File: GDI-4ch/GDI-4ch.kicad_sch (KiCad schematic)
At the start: 255 parts, among them J1 Conn_02x02_Odd_Even, J2 FTSH-107-01-F-DV-K, J3 TC2030, J4 Conn_01x06, J5 Conn_01x04, P1 368255-2, P10 Pad, P11 Pad, P18 Pad, P19 Pad, P2 Pad, P20 Pad, P25 Pad, P3 Pad, P32 Pad, P36 Pad, P4 Pad, P5 Pad, P6 Pad, P7 Pad, P8 Pad, P9 Pad, Q1 BUK9230-100B, Q10 BUK9230-100B, Q11 BUK9230-100B, Q12 BUK9230-100B, Q13 AOD4185, Q14 VND14NV04TR-E, Q15 VND14NV04TR-E, Q2 BUK9230-100B, Q3 BUK9230-100B, Q4 BUK9230-100B, Q5 BUK9230-100B, Q6 BUK9230-100B, Q7 BUK9230-100B, Q8 BUK9230-100B, Q9 BUK9230-100B, U1 MC33816, U2 TJA1051T-3, U3 LM78M05_TO252, U4 74HC14, U5 XC6206P332MR, U6 MCP6004, U7 STM32F103C8Tx, Y2 1MHz

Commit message: PCB update 6ch
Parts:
- removed R92: DNP, hellen-one-common:PAD-0805-PAD, symbol hellen-one-common:Jumper-Pad-Pad
- removed R93: Jumper-Pad-Pad, hellen-one-common:PAD-0805-PAD, symbol hellen-one-common:Jumper-Pad-Pad
- added C89: 1000pF, Capacitor_SMD:C_0603_1608Metric, symbol Device:C
- added D19: STPS2H100UY, Diode_SMD:D_SMB, symbol Device:D_Schottky_Small
- added Q16: BUK9230-100B, Package_TO_SOT_SMD:TO-252-2, symbol Device:Q_NMOS_GDS
- added R37: DNP, hellen-one-common:PAD-0805-PAD, symbol hellen-one-common:Jumper-Pad-Pad
- added R41: Jumper-Pad-Pad, hellen-one-common:PAD-0805-PAD, symbol hellen-one-common:Jumper-Pad-Pad
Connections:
- net +BATT: now also D16.1 (K)
- net L6: now also D19.2 (A), Q16.2 (D), R41.1; no longer C67.2, D16.2 (A), Q12.2 (D), R87.2, U1.33 (D_LS6)
- net Vdrive: now also D19.1 (K)
- net VSENSE2: now reaches C58.1, C61.1, Q10.3 (S), Q9.3 (S), R22.1
- net VSENSE2: now also C89.1, Q16.3 (S)
- net at C63.2, Q12.1 (G), R20.2: now also C89.2, Q16.1 (G)
- net at C63.1, Q12.3 (S), R26.1: no longer C87.1, Q1.3 (S)
- net VSENSE1: now reaches C54.1, C55.1, Q7.3 (S), Q8.3 (S), R21.1
- net VSENSE1: now also C87.1, Q1.3 (S)
- new net: R37.2, R41.2, U1.33 (D_LS6)
- new net L6PUMP: C67.2, D16.2 (A), Q12.2 (D), R37.1, R87.2
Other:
- note removed: "PUMP"
- moved on the sheet: C10, C11, C12, C13, C14, C15, C16, C17, C21, C22, C23, C24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

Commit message: Fab preview
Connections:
- no-connect marks 91 -> 92
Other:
- note removed: "INJ"
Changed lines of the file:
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@@
   (title_block
     (title "GDI 4ch")
-    (date "2022-06-30")
+    (date "2022-07-07")
     (rev "rev. c")
     (company "rusEFI.com")
@@
   (no_connect (at 546.1 129.54))
   (no_connect (at 556.26 106.68))
+  (no_connect (at 482.6 143.51))
   (no_connect (at 44.45 314.96))
   (no_connect (at 44.45 317.5))
@@
     (effects (font (size 1.524 1.524)) (justify left bottom))
   )
-  (text "INJ" (at 312.42 320.04 0)
-    (effects (font (size 1.524 1.524)) (justify left bottom))
-  )

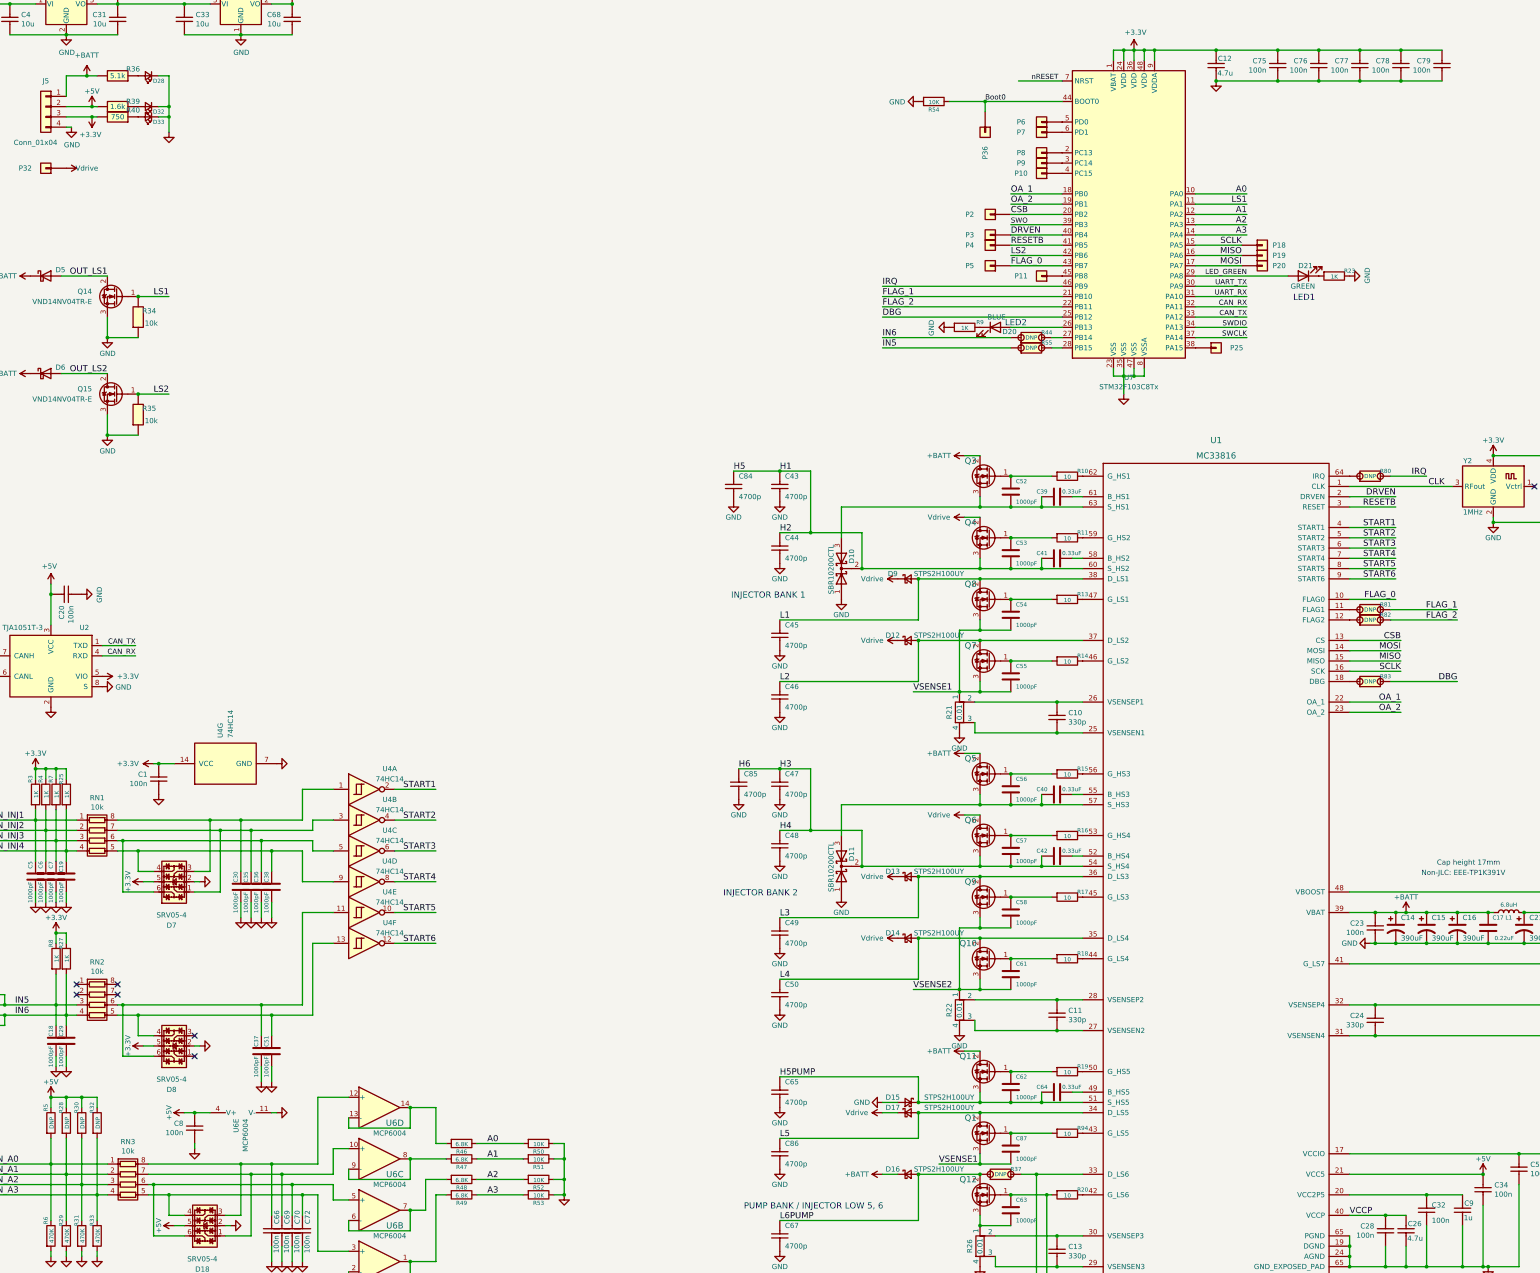
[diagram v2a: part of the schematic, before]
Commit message: Added STM32 8MHz crystal
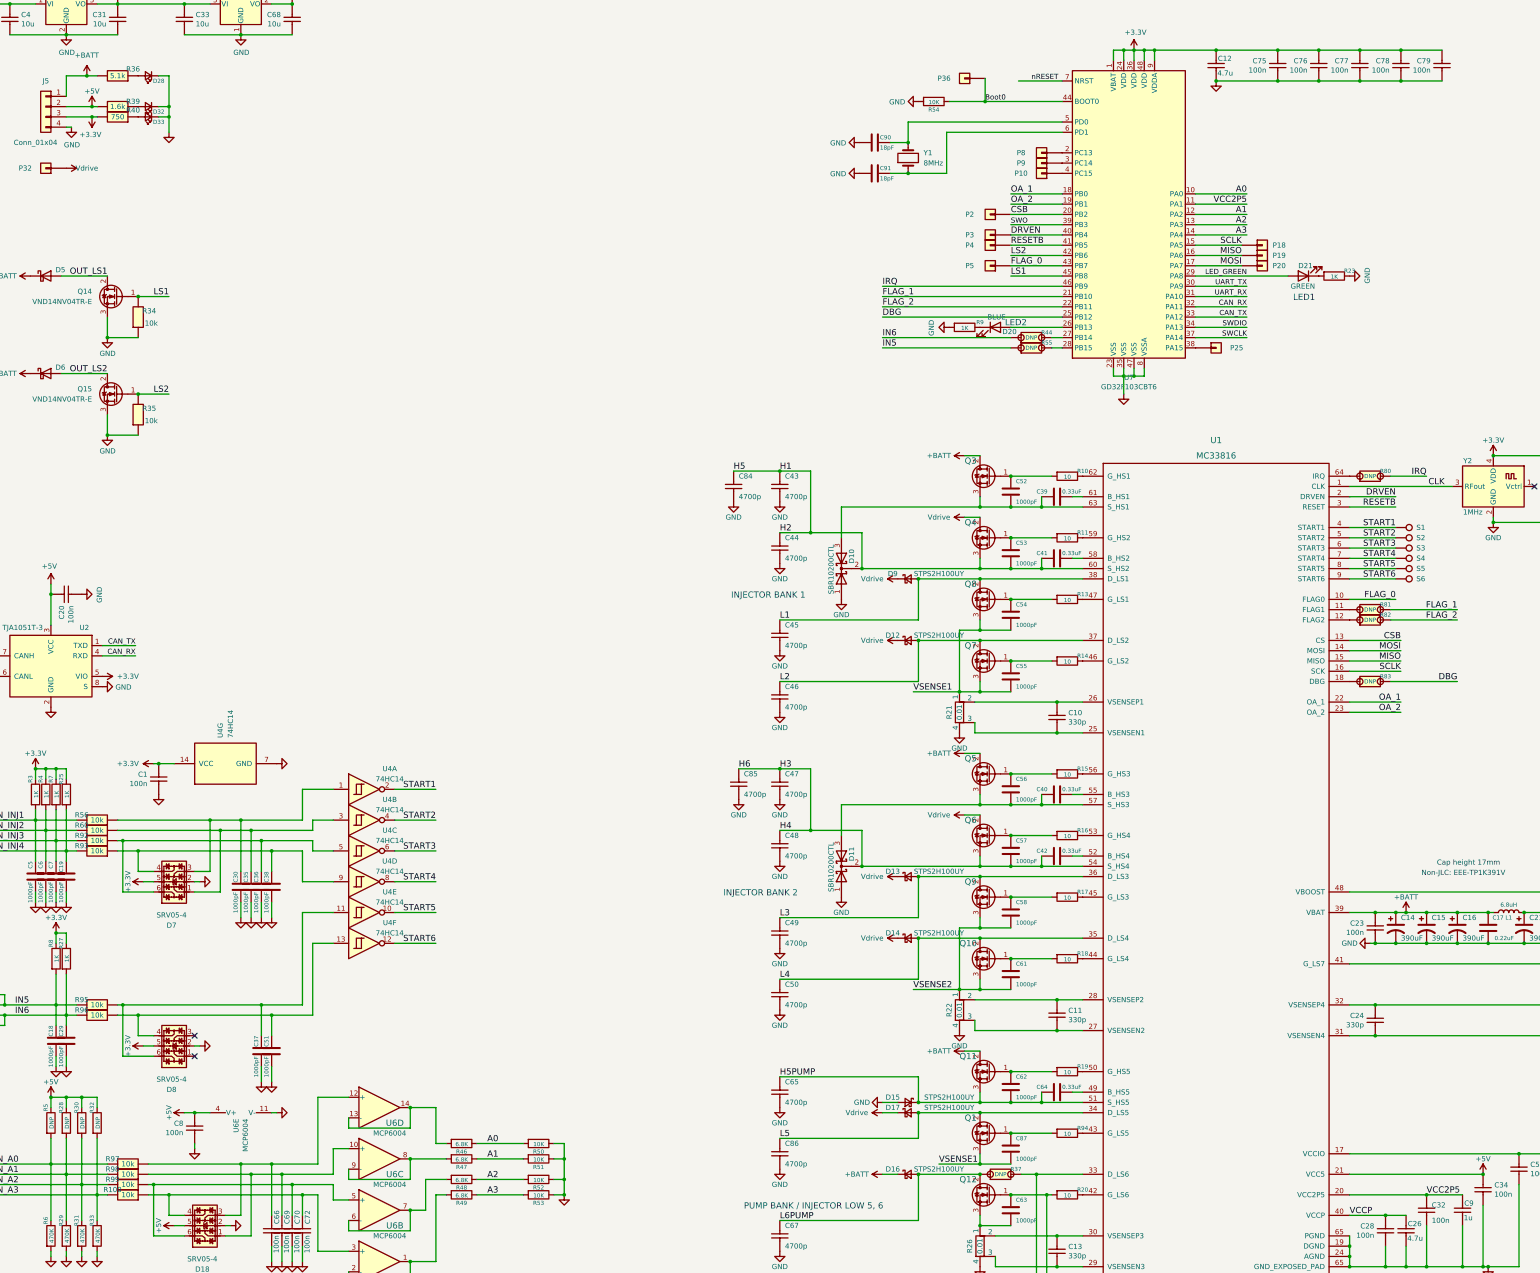
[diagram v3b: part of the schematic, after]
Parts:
- removed P11, P6, P7: Pad, hellen-one-common:PAD-TH, symbol hellen-one-common:Pad
- removed RN1, RN2, RN3: 10k, Resistor_SMD:R_Array_Convex_4x0603, symbol Device:R_Pack04
- added C90, C91: 18pF, Capacitor_SMD:C_0603_1608Metric, symbol Device:C
- added R100, R56, R60, R92, R93, R95, R96, R97, R98, R99: 10k, hellen-one-common:R0603, symbol hellen-one-common:Res
- added S1, S2, S3, S4, S5, S6: TestPoint, TestPoint:TestPoint_Pad_D1.5mm, symbol Connector:TestPoint
- added Y1: 8MHz, Crystal:Crystal_SMD_HC49-SD, symbol Device:Crystal
- U7: value STM32F103C8Tx -> GD32F103CBT6; LCSC C8734 -> C77979
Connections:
- net GND: now also C90.2, C91.2
- net IN5: now also R95.2
- net IN6: now also R96.2
- net IN_A0: now also R97.2
- net IN_A1: now also R98.2
- net IN_A2: now also R99.2
- net IN_A3: now also R100.2
- net IN_INJ1: now also R56.2
- net IN_INJ2: now also R60.2
- net IN_INJ3: now also R92.2
- net IN_INJ4: now also R93.2
- net LS1: now also U7.45 (PB8); no longer U7.11 (PA1)
- net START1: now also S1.1
- net START2: now also S2.1
- net START3: now also S3.1
- net START4: now also S4.1
- net START5: now also S5.1
- net START6: now also S6.1
- net at C51.2, D8.4, U4.13: now also R96.1
- net at C72.2, D18.4, U6.3 (+): now also R100.1
- net at C35.2, D7.1, U4.3: now also R60.1
- net at C30.2, D7.3, U4.1: now also R56.1
- net at C38.2, D7.4, U4.9: now also R93.1
- net at C36.2, D7.6, U4.5: now also R92.1
- net at U7.6 (PD1): now also C91.1, Y1.1
- net at C37.2, D8.6, U4.11: now also R95.1
- net VCC2P5: now reaches C32.2, C9.2, U1.20 (VCC2P5)
- net VCC2P5: now also U7.11 (PA1)
- net at C69.2, D18.1, U6.10 (+): now also R98.1
- net at C66.2, D18.3, U6.12 (+): now also R97.1
- net at C70.2, D18.6, U6.5 (+): now also R99.1
- net at U7.5 (PD0): now also C90.1, Y1.2
- no-connect marks 92 -> 88
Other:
- moved on the sheet: P36

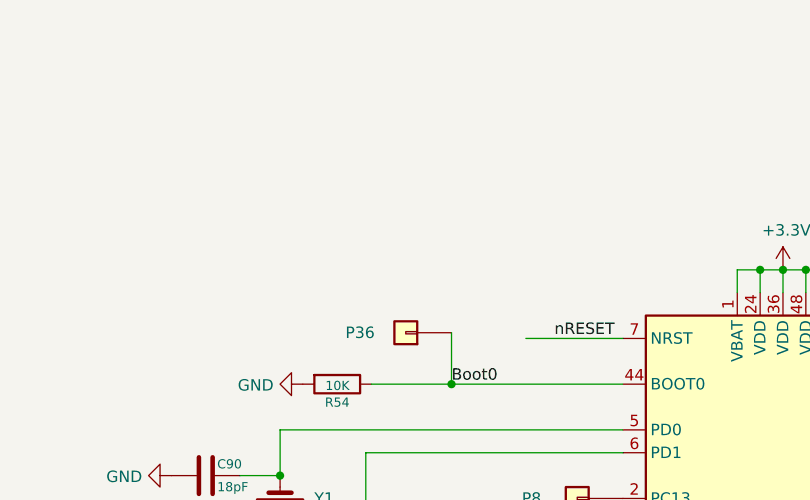
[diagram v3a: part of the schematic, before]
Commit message: BOOT and RST buttons
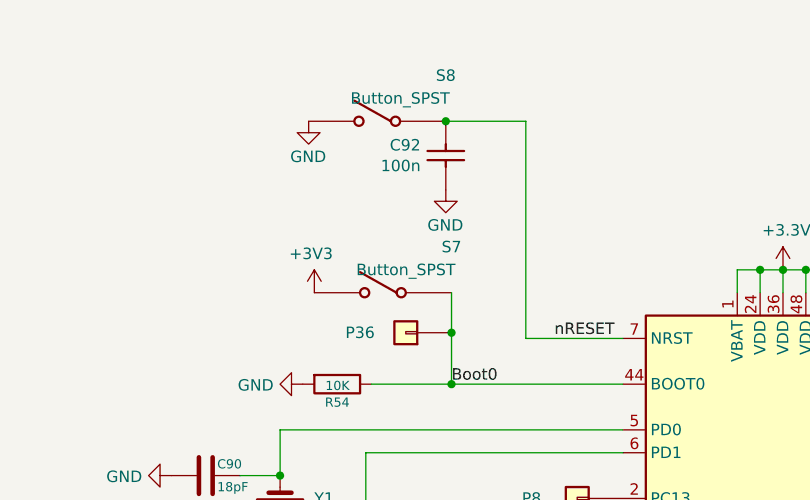
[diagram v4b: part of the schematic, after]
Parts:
- added C92: 100n, hellen-one-common:C0603, symbol hellen-one-common:Cap
- added S7, S8: Button_SPST, hellen-one-common:SMD-2_2.9x3.9x1.7, symbol hellen-one-common:Button_SPST
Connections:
- net +3V3: now also S7.2
- net Boot0: now also S7.1
- net GND: now also C92.1, S8.2
- net nRESET: now also C92.2, S8.1
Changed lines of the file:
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@@
   (title_block
     (title "GDI 4ch")
-    (date "2022-07-07")
+    (date "2022-07-18")
     (rev "rev. c")
     (company "rusEFI.com")
@@
   (junction (at 204.47 309.88) (diameter 0) (color 0 0 0 0)
   )
+  (junction (at 346.71 42.545) (diameter 0) (color 0 0 0 0)
+  )
   (junction (at 162.56 311.15) (diameter 0) (color 0 0 0 0)
   )
@@
   (junction (at 167.64 231.14) (diameter 0) (color 0 0 0 0)
   )
+  (junction (at 346.075 19.05) (diameter 0) (color 0 0 0 0)
+  )
   (junction (at 455.93 336.55) (diameter 0) (color 0 0 0 0)
   )
@@
     (stroke (width 0) (type default) (color 0 0 0 0))
   )
+  (wire (pts (xy 354.965 19.05) (xy 354.965 43.18))
+    (stroke (width 0) (type default) (color 0 0 0 0))
+  )
   (wire (pts (xy 321.31 106.68) (xy 353.06 106.68))
     (stroke (width 0) (type default) (color 0 0 0 0))
@@
     (stroke (width 0) (type default) (color 0 0 0 0))
   )
+  (wire (pts (xy 346.075 19.05) (xy 354.965 19.05))
+    (stroke (width 0) (type default) (color 0 0 0 0))
+  )
   (wire (pts (xy 556.26 82.55) (xy 565.15 82.55))
     (stroke (width 0) (type default) (color 0 0 0 0))
@@
     (stroke (width 0) (type default) (color 0 0 0 0))
   )
+  (wire (pts (xy 346.71 38.1) (xy 346.71 42.545))
+    (stroke (width 0) (type default) (color 0 0 0 0))
+  )
   (wire (pts (xy 127 24.13) (xy 132.08 24.13))
     (stroke (width 0) (type default) (color 0 0 0 0))
@@
     (pin "1")
   )
+  (symbol (lib_id "power:+3V3") (at 331.47 38.1 0) (mirror y) (unit 1)
+    (in_bom yes) (on_board yes)
+    (property "Reference" "#PWR079" (id 0) (at 331.47 41.91 0)
+      (effects (font (size 1.27 1.27)) hide)
+    )
+    (property "Value" "+3V3" (id 1) (at 331.1017 33.7756 0))
+    (property "Footprint" "" (id 2) (at 331.47 38.1 0)
+      (effects (font (size 1.27 1.27)) hide)
+    )
+    (property "Datasheet" "" (id 3) (at 331.47 38.1 0)
+      (effects (font (size 1.27 1.27)) hide)
+    )
+    (pin "1")
+  )
   (symbol (lib_id "Device:D_Schottky_Small") (at 327.66 344.17 0) (unit 1)
     (in_bom yes) (on_board yes)
@@
     (pin "2")
   )
+  (symbol (lib_id "hellen-one-common:Cap") (at 346.075 22.86 270) (mirror x) (unit 1)
+    (in_bom yes) (on_board yes)
+    (property "Reference" "C92" (id 0) (at 343.2809 21.7106 90)
+      (effects (font (size 1.27 1.27)) (justify right))
+    )
+    (property "Value" "100n" (id 1) (at 343.2809 24.0093 90)
+      (effects (font (size 1.27 1.27)) (justify right))
+    )
+    (property "Footprint" "hellen-one-common:C0603" (id 2) (at 342.265 25.4 0)
+      (effects (font (size 1.27 1.27)) hide)
+    )
+    (property "Datasheet" "" (id 3) (at 346.075 26.67 90)
+      (effects (font (size 1.27 1.27)) hide)
+    )
+    (property "LCSC" "C14663" (id 4) (at 346.075 22.86 0)
+      (effects (font (size 1.27 1.27)) hide)
+    )
+    (pin "1")
+    (pin "2")
+  )
   (symbol (lib_id "power:+5V") (at 568.325 60.325 0) (unit 1)
     (in_bom yes) (on_board yes)
@@
     (pin "1")
   )
+  (symbol (lib_id "hellen-one-common:Button_SPST") (at 340.995 16.51 0) (mirror y) (unit 1)
+    (in_bom yes) (on_board yes)
+    (property "Reference" "S8" (id 0) (at 346.075 13.97 0))
+    (property "Value" "Button_SPST" (id 1) (at 340.995 16.51 0))
+    (property "Footprint" "hellen-one-common:SMD-2_2.9x3.9x1.7" (id 2) (at 340.995 16.51 0)
+      (effects (font (size 1.27 1.27)) hide)
+    )
+    (property "Datasheet" "" (id 3) (at 340.995 16.51 0)
+      (effects (font (size 1.27 1.27)) hide)
+    )
+    (property "LCSC" "C115357" (id 4) (at 340.995 16.51 0)
+      (effects (font (size 1.27 1.27)) hide)
+    )
+    (pin "1")
+    (pin "2")
+  )
   (symbol (lib_id "Connector_Generic:Conn_01x04") (at 114.3 49.53 0) (mirror y) (unit 1)
     (in_bom yes) (on_board yes)
@@
     (pin "2")
   )
+  (symbol (lib_id "hellen-one-common:Button_SPST") (at 341.63 35.56 0) (mirror y) (unit 1)
+    (in_bom yes) (on_board yes)
+    (property "Reference" "S7" (id 0) (at 346.71 33.02 0))
+    (property "Value" "Button_SPST" (id 1) (at 341.63 35.56 0))
+    (property "Footprint" "hellen-one-common:SMD-2_2.9x3.9x1.7" (id 2) (at 341.63 35.56 0)
+      (effects (font (size 1.27 1.27)) hide)
+    )
+    (property "Datasheet" "" (id 3) (at 341.63 35.56 0)
+      (effects (font (size 1.27 1.27)) hide)
+    )
+    (property "LCSC" "C115357" (id 4) (at 341.63 35.56 0)
+      (effects (font (size 1.27 1.27)) hide)
+    )
+    (pin "1")
+    (pin "2")
+  )
   (symbol (lib_id "Device:D_TVS") (at 78.74 33.02 270) (unit 1)
     (in_bom yes) (on_board yes)
@@
     (pin "1")
   )
+  (symbol (lib_id "power:GND") (at 346.075 26.67 0) (mirror y) (unit 1)
+    (in_bom yes) (on_board yes)
+    (property "Reference" "#PWR081" (id 0) (at 346.075 33.02 0)
+      (effects (font (size 1.27 1.27)) hide)
+    )
+    (property "Value" "GND" (id 1) (at 346.0242 30.6134 0))
+    (property "Footprint" "" (id 2) (at 346.075 26.67 0)
+      (effects (font (size 1.27 1.27)) hide)
+    )
+    (property "Datasheet" "" (id 3) (at 346.075 26.67 0)
+      (effects (font (size 1.27 1.27)) hide)
+    )
+    (pin "1")
+  )
   (symbol (lib_id "power:+5V") (at 115.57 294.64 0) (unit 1)
     (in_bom yes) (on_board yes)
@@
     (pin "2")
   )
+  (symbol (lib_id "power:GND") (at 330.835 19.05 0) (mirror y) (unit 1)
+    (in_bom yes) (on_board yes)
+    (property "Reference" "#PWR080" (id 0) (at 330.835 25.4 0)
+      (effects (font (size 1.27 1.27)) hide)
+    )
+    (property "Value" "GND" (id 1) (at 330.7842 22.9934 0))
+    (property "Footprint" "" (id 2) (at 330.835 19.05 0)
+      (effects (font (size 1.27 1.27)) hide)
+    )
+    (property "Datasheet" "" (id 3) (at 330.835 19.05 0)
+      (effects (font (size 1.27 1.27)) hide)
+    )
+    (pin "1")
+  )
   (symbol (lib_id "power:+3.3V") (at 383.54 35.56 0) (unit 1)
     (in_bom yes) (on_board yes)
@@
       (reference "#PWR078") (unit 1) (value "GND") (footprint "")
     )
+    (path "/1ef18535-fc99-4579-8385-662f2e8f36e3"
+      (reference "#PWR079") (unit 1) (value "+3V3") (footprint "")
+    )
+    (path "/c8efac96-3fce-4a1f-a420-6abcfc72bf5d"
+      (reference "#PWR080") (unit 1) (value "GND") (footprint "")
+    )
+    (path "/b581c905-09d3-4d38-82c9-6cec6503acff"
+      (reference "#PWR081") (unit 1) (value "GND") (footprint "")
+    )
     (path "/b26bffed-114b-42d6-86b2-43be466c5614"
       (reference "#PWR0101") (unit 1) (value "GND") (footprint "")
@@
       (reference "C91") (unit 1) (value "18pF") (footprint "Capacitor_SMD:C_0603_1608Metric")
     )
+    (path "/4d7b888b-efca-4575-b5da-d7e11fa1f75e"
+      (reference "C92") (unit 1) (value "100n") (footprint "hellen-one-common:C0603")
+    )
     (path "/7ead9a68-478f-4d7a-ae38-b5e9199b6126"
       (reference "D1") (unit 1) (value "SMCJ22CA") (footprint "Diode_SMD:D_SMC")
@@
       (reference "S6") (unit 1) (value "TestPoint") (footprint "TestPoint:TestPoint_Pad_D1.5mm")
     )
+    (path "/7dbe58a3-cbbc-4229-8367-bf78e2a0ac12"
+      (reference "S7") (unit 1) (value "Button_SPST") (footprint "hellen-one-common:SMD-2_2.9x3.9x1.7")
+    )
+    (path "/55bfb56d-0a6f-4679-ad43-a2e436486b48"
+      (reference "S8") (unit 1) (value "Button_SPST") (footprint "hellen-one-common:SMD-2_2.9x3.9x1.7")
+    )
     (path "/68d2e4d4-c26a-4ee5-96f0-3e8f7619ca46"
